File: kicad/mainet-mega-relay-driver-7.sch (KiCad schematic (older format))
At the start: 8 parts, among them J36 Screw_Terminal_01x03, K7 SANYOU_SRD_Form_C, Q7 2N3904, U8 4N37

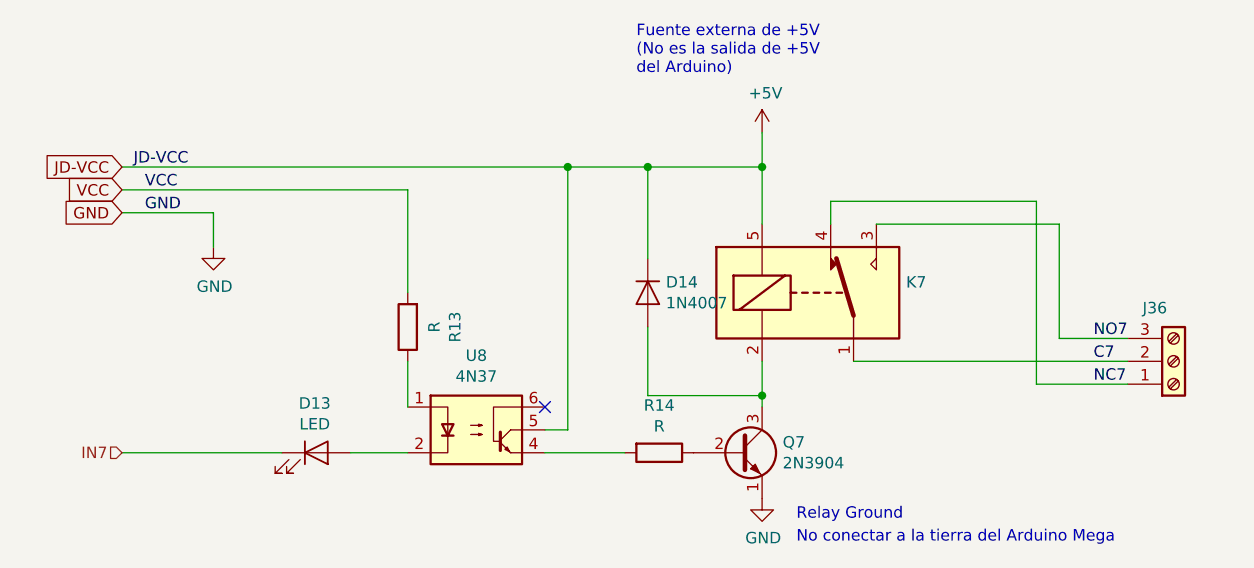
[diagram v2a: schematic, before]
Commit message: KICAD: Actualización de esquematicos del módulo de 8 relés de control
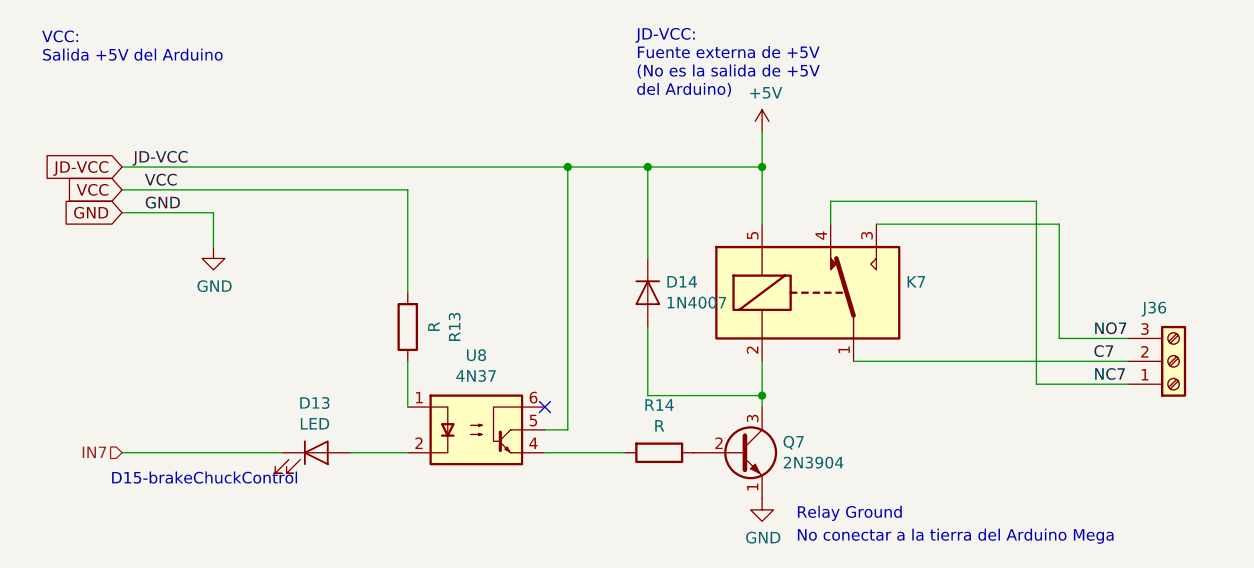
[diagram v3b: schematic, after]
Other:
- note added: "D15-brakeChuckControl"
- note added: "JD-VCC:\nFuente externa de +5V\n(No es la salida de +5V \ndel Arduino)"
- note added: "VCC:\nSalida +5V del Arduino"
- note removed: "Fuente externa de +5V\n(No es la salida de +5V \ndel Arduino)"
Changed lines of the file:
@@
 EESchema Schematic File Version 4
 LIBS:mainet-mega-cache
-LIBS:mainet-mega-5V-to-mp-10v-cache
 EELAYER 30 0
 EELAYER END
 $Descr A4 11693 8268
 encoding utf-8
-Sheet 12 21
-Title ""
-Date ""
+Sheet 13 21
+Title "Relay driver 7"
+Date "2021-02-02"
 Rev ""
 Comp ""
@@
 	1    0    0    -1
 $EndComp
-Text Notes 6050 2550 0    50   ~ 0
-Fuente externa de +5V\n(No es la salida de +5V \ndel Arduino)
 Text Notes 6750 4500 0    50   ~ 0
 Relay Ground\n
@@
 Text GLabel 3800 3150 0    50   Input ~ 0
 GND
+Text Notes 6050 2650 0    50   ~ 0
+JD-VCC:\nFuente externa de +5V\n(No es la salida de +5V \ndel Arduino)
+Text Notes 3450 2500 0    50   ~ 0
+VCC:\nSalida +5V del Arduino
+Text Notes 3750 4350 0    50   ~ 0
+D15-brakeChuckControl
 $EndSCHEMATC
